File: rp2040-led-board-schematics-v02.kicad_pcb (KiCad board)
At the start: 4 copper layers, 228 x 98 mm, 287 parts, among them J1 ReceiverRS485, J10 Terminal, J11 ReceiverData, J12 ReceiverData, J13 ReceiverData, J14 ReceiverData, J15 ReceiverRS485, J16 ReceiverRS485, J17 ReceiverRS485, J18 ReceiverRS485, J19 Terminal, J2 ReceiverRS485, J20 Terminal, J21 Terminal, J22 Terminal, J23 ReceiverData, J24 ReceiverData, J25 ReceiverData, J26 ReceiverData, J27 MainBoard, J3 ReceiverRS485, J4 ReceiverRS485, J5 PWR_IN, J6 Terminal, J7 Terminal, J8 Terminal, J9 FrontPanel, SW1 PEC16, SW2 Button, U10 MAX485EE, U11 MAX485EE, U12 MAX485EE, U13 MAX485EE, U14 Pico, U15 MAX485EE, U16 MAX485EE, U17 AMS1117-5.0, U21 MAX485EE, U22 MAX485EE, U23 MAX485EE, U24 MAX485EE, U25 MAX485EE, U26 MAX485EE, U27 ENC28J60, U29 AMS1117-5.0, U30 AMS1117-5.0, U31 AMS1117-5.0, U32 AMS1117-5.0, U33 AMS1117-5.0, U34 AMS1117-5.0, U35 AMS1117-5.0, U5 NCP1117LP, U6 MAX485EE, U7 MAX485EE, U8 MAX485EE, U9 MAX485EE

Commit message: should be ready to find parts
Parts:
- removed C16: 220nF, Capacitor_SMD:C_0603_1608Metric
- removed JP5: 12V, Jumper:SolderJumper-2_P1.3mm_Open_Pad1.0x1.5mm
- removed U5: NCP1117LP, Package_TO_SOT_SMD:SOT-223
- added C71: 100nF, Capacitor_SMD:C_0603_1608Metric, F.Cu at (68.0, 80.3)
- added C72: 100nF, Capacitor_SMD:C_0402_1005Metric, F.Cu at (63.0, 77.0)
- added C74: 10uF, Capacitor_SMD:C_1206_3216Metric, F.Cu at (60.0, 73.5)
- added F1: 1A, Fuse:Fuse_1206_3216Metric, F.Cu at (59.8, 64.3)
- added FB2: 600 @ 600Mhz, Inductor_SMD:L_0805_2012Metric, F.Cu at (71.5, 80.6)
- added JPe: 12V, Jumper:SolderJumper-2_P1.3mm_Open_Pad1.0x1.5mm, F.Cu at (56.4, 68.0)
- added L1: 5.6mH 120mOhm, Inductor_SMD:L_Sunlord_MWSA0503S, F.Cu at (69.0, 74.0)
- added Q1: AO3401A, Package_TO_SOT_SMD:SOT-23, F.Cu at (49.9, 69.5)
- added U2: LMR50410Y5FQDBVRQ1, Package_TO_SOT_SMD:SOT-23-6, F.Cu at (63.9, 79.5)
- C11: value 100nF -> 1uF
- moved JP10 22.1 mm to (55.0, 63.0), turned to 180 degrees
- moved C11 11.2 mm to (69.8, 80.3), turned to -90 degrees
- moved H13 8.26 mm to (55.0, 98.0)
- moved J9 4.34 mm to (47.0, 75.3)
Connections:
- C11 pad 1: Net-(JP5-A) -> /Buck in
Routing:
- net Net-(Q1-S): track 0.00 -> 35.5 mm
- net /Buck out: track 0.00 -> 20.1 mm
- net Net-(Q1-D): track 0.00 -> 11.5 mm
- net Net-(J5-Pin_2): track 23.8 -> 14.9 mm
- net Net-(JP5-A): track 6.62 -> 0.00 mm
- net /Receiver 7/12V: track 0.00 -> 6.52 mm
- net /Receiver 5/12V: track 0.00 -> 6.52 mm
- net /Receiver 3/12V: track 0.00 -> 6.52 mm
- net /Receiver 2/12V: track 0.00 -> 6.52 mm
- net /Receiver 1/12V: track 0.00 -> 6.52 mm
- net /Receiver 8/12V: track 0.00 -> 6.52 mm
- net /Receiver 6/12V: track 0.00 -> 6.52 mm
- net /Receiver 4/12V: track 0.00 -> 6.52 mm
- net MBSwitchPush: track 156.6 -> 151.1 mm
- net MBEncoderS: track 104.6 -> 99.5 mm
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- added copper zone on F.Cu, net /Buck in
- added copper zone on F.Cu, net /Buck out
- added copper zone on F.Cu, net /SW
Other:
- board text added: "LED2 STRIP"
- board text added: "LED2-"
- board text added: "LED3 STRIP"
- board text added: "LED3-"
- board text added: "LED4 STRIP"
- board text added: "LED4-"
- board text added: "LED5 STRIP"
- board text added: "LED5-"
- board text added: "LED6 STRIP"
- board text added: "LED6-"
- board text added: "LED7 STRIP"
- board text added: "LED7-"
- board text added: "LED8 STRIP"
- board text added: "LED8-"

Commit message: fix: update .svg & .png files, correct some silkscreen details
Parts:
- moved H34 1.41 mm to (253.5, 70.9)
- moved H35 1.41 mm to (230.5, 70.9)
- moved H36 1.41 mm to (207.5, 70.9)
- moved H37 1.41 mm to (184.5, 71.0)
- moved H38 1.41 mm to (253.5, 114.0)
- moved H39 1.41 mm to (230.5, 114.0)
- moved H40 1.41 mm to (207.5, 114.0)
- moved H41 1.41 mm to (184.5, 114.0)
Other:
- board text added: "LED BOARD [receiver1] v1 - jan 2024"
- board text added: "LED BOARD [receiver2] v1 - jan 2024"
- board text added: "LED BOARD [receiver3] v1 - jan 2024"
- board text added: "LED BOARD [receiver4] v1 - jan 2024"
- board text added: "LED BOARD [receiver5] v1 - jan 2024"
- board text added: "LED BOARD [receiver6] v1 - jan 2024"
- board text added: "LED BOARD [receiver7] v1 - jan 2024"
- board text added: "LED BOARD [receiver8] v1 - jan 2024"
- board text removed: "LED BOARD [receiver] v1 - jan 2024"
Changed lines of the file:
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@@
   )
   (footprint "Frangitron:frangitron_logo_16mm" (layer "B.Cu")
-    (at 185.5 113 90)
+    (at 184.500001 114 90)
     (property "Sheetfile" "Receiver.kicad_sch")
     (property "Sheetname" "Receiver 1")
@@
   )
   (footprint "Frangitron:frangitron_logo_16mm" (layer "B.Cu")
-    (at 185.499999 70 90)
+    (at 184.5 71 90)
     (property "Sheetfile" "Receiver.kicad_sch")
     (property "Sheetname" "Receiver 2")
@@
   )
   (footprint "Frangitron:frangitron_logo_16mm" (layer "B.Cu")
-    (at 254.499999 69.925001 90)
+    (at 253.5 70.925001 90)
     (property "Sheetfile" "Receiver.kicad_sch")
     (property "Sheetname" "Receiver 8")
@@
   )
   (footprint "Frangitron:frangitron_logo_16mm" (layer "B.Cu")
-    (at 231.499999 69.925001 90)
+    (at 230.5 70.925001 90)
     (property "Sheetfile" "Receiver.kicad_sch")
     (property "Sheetname" "Receiver 6")
@@
   )
   (footprint "Frangitron:frangitron_logo_16mm" (layer "B.Cu")
-    (at 231.499999 113 90)
+    (at 230.5 114 90)
     (property "Sheetfile" "Receiver.kicad_sch")
     (property "Sheetname" "Receiver 5")
@@
   )
   (footprint "Frangitron:frangitron_logo_16mm" (layer "B.Cu")
-    (at 208.499999 69.925001 90)
+    (at 207.5 70.925001 90)
     (property "Sheetfile" "Receiver.kicad_sch")
     (property "Sheetname" "Receiver 4")
@@
   )
   (footprint "Frangitron:frangitron_logo_16mm" (layer "B.Cu")
-    (at 208.499999 113 90)
+    (at 207.5 114 90)
     (property "Sheetfile" "Receiver.kicad_sch")
     (property "Sheetname" "Receiver 3")
@@
   )
   (footprint "Frangitron:frangitron_logo_16mm" (layer "B.Cu")
-    (at 254.499999 113 90)
+    (at 253.5 114 90)
     (property "Sheetfile" "Receiver.kicad_sch")
     (property "Sheetname" "Receiver 7")
@@
   (gr_arc locked (start 144.999999 134) (mid 143.24264 138.242641) (end 138.999999 140)
     (stroke (width 0.1) (type default)) (layer "User.2"))
+  (gr_text "LED BOARD [receiver2]\nv1 - jan 2024" (at 180.000001 78.5 270) (layer "B.SilkS")
+    (effects (font (size 0.8 0.8) (thickness 0.15)) (justify left bottom mirror))
+  )
+  (gr_text "LED BOARD [receiver6]\nv1 - jan 2024" (at 226.000001 78.5 270) (layer "B.SilkS")
+    (effects (font (size 0.8 0.8) (thickness 0.15)) (justify left bottom mirror))
+  )
+  (gr_text "LED BOARD [receiver4]\nv1 - jan 2024" (at 203.000001 78.5 270) (layer "B.SilkS")
+    (effects (font (size 0.8 0.8) (thickness 0.15)) (justify left bottom mirror))
+  )
+  (gr_text "LED BOARD [receiver7]\nv1 - jan 2024" (at 249.000001 121.5 270) (layer "B.SilkS")
+    (effects (font (size 0.8 0.8) (thickness 0.15)) (justify left bottom mirror))
+  )
+  (gr_text "LED BOARD [receiver3]\nv1 - jan 2024" (at 203.000001 121.5 270) (layer "B.SilkS")
+    (effects (font (size 0.8 0.8) (thickness 0.15)) (justify left bottom mirror))
+  )
   (gr_text "LED BOARD [front panel]\nv1 - jan 2024" (at 172.999999 113.461592 90) (layer "B.SilkS")
     (effects (font (size 0.8 0.8) (thickness 0.15)) (justify left bottom mirror))
   )
-  (gr_text "LED BOARD [receiver]\nv1 - jan 2024" (at 180.999999 120.499999 -90) (layer "B.SilkS")
+  (gr_text "LED BOARD [receiver8]\nv1 - jan 2024" (at 249.000001 78.5 270) (layer "B.SilkS")
+    (effects (font (size 0.8 0.8) (thickness 0.15)) (justify left bottom mirror))
+  )
+  (gr_text "LED BOARD [receiver5]\nv1 - jan 2024" (at 226.000001 121.5 270) (layer "B.SilkS")
+    (effects (font (size 0.8 0.8) (thickness 0.15)) (justify left bottom mirror))
+  )
+  (gr_text "LED BOARD [receiver1]\nv1 - jan 2024" (at 180 121.499999 270) (layer "B.SilkS")
     (effects (font (size 0.8 0.8) (thickness 0.15)) (justify left bottom mirror))
   )

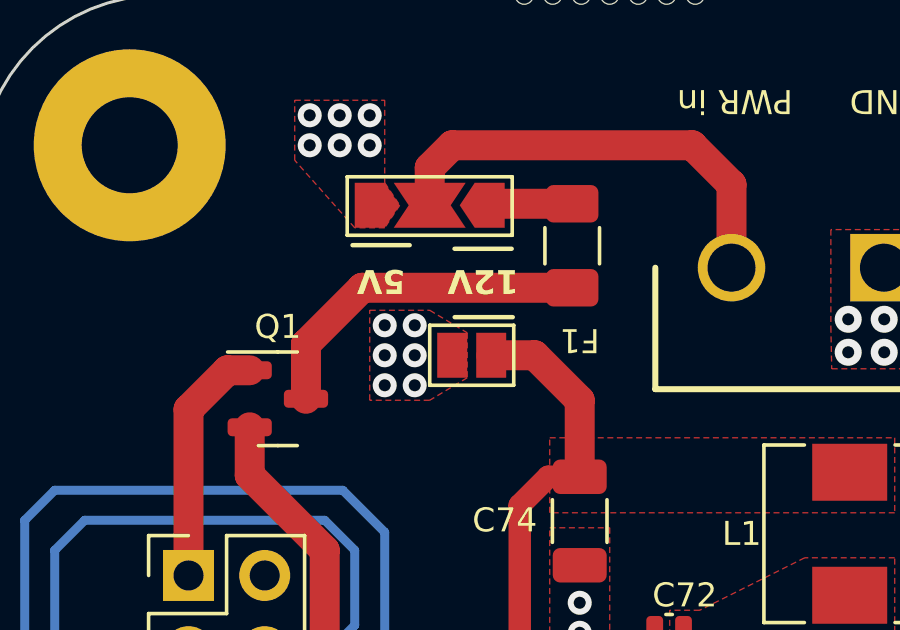
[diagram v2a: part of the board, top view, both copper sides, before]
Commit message: fix: DRC & ERC revealed designators were out of sync between schem and pcb
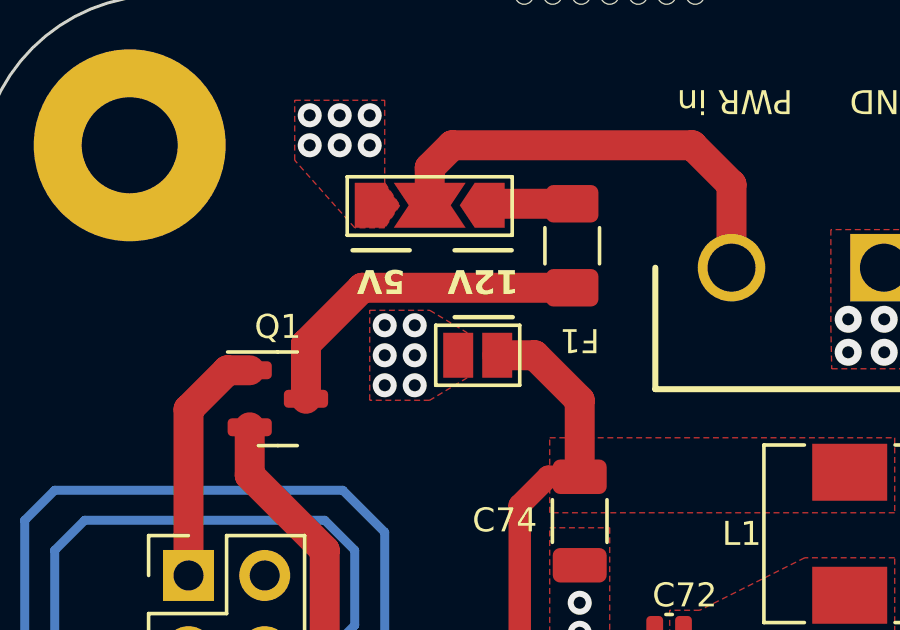
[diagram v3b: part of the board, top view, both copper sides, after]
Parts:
- removed JPe: 12V, Jumper:SolderJumper-2_P1.3mm_Open_Pad1.0x1.5mm
- added JP5: 12V, Jumper:SolderJumper-2_P1.3mm_Open_Pad1.0x1.5mm, F.Cu at (56.6, 68.0)
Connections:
- net Net-(U2-CB) renamed /CB
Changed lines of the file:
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@@
   (net 156 "/Receiver 7/LDO OUT")
   (net 157 "/Buck in")
-  (net 158 "Net-(U2-CB)")
+  (net 158 "/CB")
   (net 159 "/Buck out")
   (net 160 "Net-(Q1-S)")
@@
       (net 162 "/SW") (pintype "passive"))
     (pad "2" smd roundrect (at 0.48 0 180) (size 0.56 0.62) (layers "F.Cu" "F.Paste" "F.Mask") (roundrect_rratio 0.25)
-      (net 158 "Net-(U2-CB)") (pintype "passive"))
+      (net 158 "/CB") (pintype "passive"))
     (model "${KICAD6_3DMODEL_DIR}/Capacitor_SMD.3dshapes/C_0402_1005Metric.wrl"
       (offset (xyz 0 0 0))
@@
       (net 11 "/FP GND") (pinfunction "1") (pintype "input"))
   )
-  (footprint "Jumper:SolderJumper-2_P1.3mm_Open_Pad1.0x1.5mm" (layer "F.Cu")
-    (at 56.4 68 180)
-    (descr "SMD Solder Jumper, 1x1.5mm Pads, 0.3mm gap, open")
-    (tags "solder jumper open")
-    (property "Sheetfile" "rp2040-led-board-schematics-v02.kicad_sch")
-    (property "Sheetname" "")
-    (property "URL" "")
-    (property "ki_description" "Solder Jumper, 2-pole, open")
-    (property "ki_keywords" "solder jumper SPST")
-    (attr exclude_from_pos_files)
-    (fp_text reference "JPe" (at 0 -1.8) (layer "F.SilkS") hide
-        (effects (font (size 0.8 0.8) (thickness 0.15)))
-    )
-    (fp_text value "12V" (at 0 1.9) (layer "F.Fab")
-        (effects (font (size 0.8 0.8) (thickness 0.15)))
-    )
-    (fp_line (start -1.4 -1) (end 1.4 -1)
-      (stroke (width 0.12) (type solid)) (layer "F.SilkS"))
-    (fp_line (start -1.4 1) (end -1.4 -1)
-      (stroke (width 0.12) (type solid)) (layer "F.SilkS"))
-    (fp_line (start 1.4 -1) (end 1.4 1)
-      (stroke (width 0.12) (type solid)) (layer "F.SilkS"))
-    (fp_line (start 1.4 1) (end -1.4 1)
-      (stroke (width 0.12) (type solid)) (layer "F.SilkS"))
-    (fp_line (start -1.65 -1.25) (end -1.65 1.25)
-      (stroke (width 0.05) (type solid)) (layer "F.CrtYd"))
-    (fp_line (start -1.65 -1.25) (end 1.65 -1.25)
-      (stroke (width 0.05) (type solid)) (layer "F.CrtYd"))
-    (fp_line (start 1.65 1.25) (end -1.65 1.25)
-      (stroke (width 0.05) (type solid)) (layer "F.CrtYd"))
-    (fp_line (start 1.65 1.25) (end 1.65 -1.25)
-      (stroke (width 0.05) (type solid)) (layer "F.CrtYd"))
-    (pad "1" smd rect (at -0.65 0 180) (size 1 1.5) (layers "F.Cu" "F.Mask")
-      (net 159 "/Buck out") (pinfunction "A") (pintype "passive"))
-    (pad "2" smd rect (at 0.65 0 180) (size 1 1.5) (layers "F.Cu" "F.Mask")
-      (net 41 "+5V") (pinfunction "B") (pintype "passive"))
-  )
   (footprint "Resistor_SMD:R_0402_1005Metric" (layer "F.Cu")
     (at 130.715999 106.753 90)
@@
       (stroke (width 0.1) (type solid)) (layer "F.Fab"))
     (pad "1" smd roundrect (at -1.1375 -0.95) (size 1.325 0.6) (layers "F.Cu" "F.Paste" "F.Mask") (roundrect_rratio 0.25)
-      (net 158 "Net-(U2-CB)") (pinfunction "CB") (pintype "power_in"))
+      (net 158 "/CB") (pinfunction "CB") (pintype "power_in"))
     (pad "2" smd roundrect (at -1.1375 0) (size 1.325 0.6) (layers "F.Cu" "F.Paste" "F.Mask") (roundrect_rratio 0.25)
       (net 2 "GND") (pinfunction "GND") (pintype "power_in"))
@@
     )
   )
+  (footprint "Jumper:SolderJumper-2_P1.3mm_Open_Pad1.0x1.5mm" (layer "F.Cu")
+    (at 56.6 68 180)
+    (descr "SMD Solder Jumper, 1x1.5mm Pads, 0.3mm gap, open")
+    (tags "solder jumper open")
+    (property "Sheetfile" "rp2040-led-board-schematics-v02.kicad_sch")
+    (property "Sheetname" "")
+    (property "URL" "")
+    (property "ki_description" "Solder Jumper, 2-pole, open")
+    (property "ki_keywords" "solder jumper SPST")
+    (attr exclude_from_pos_files)
+    (fp_text reference "JP5" (at 0 -1.8) (layer "F.SilkS") hide
+        (effects (font (size 1 1) (thickness 0.15)))
+    )
+    (fp_text value "12V" (at 0 1.9) (layer "F.Fab")
+        (effects (font (size 1 1) (thickness 0.15)))
+    )
+    (fp_line (start -1.4 -1) (end 1.4 -1)
+      (stroke (width 0.12) (type solid)) (layer "F.SilkS"))
+    (fp_line (start -1.4 1) (end -1.4 -1)
+      (stroke (width 0.12) (type solid)) (layer "F.SilkS"))
+    (fp_line (start 1.4 -1) (end 1.4 1)
+      (stroke (width 0.12) (type solid)) (layer "F.SilkS"))
+    (fp_line (start 1.4 1) (end -1.4 1)
+      (stroke (width 0.12) (type solid)) (layer "F.SilkS"))
+    (fp_line (start -1.65 -1.25) (end -1.65 1.25)
+      (stroke (width 0.05) (type solid)) (layer "F.CrtYd"))
+    (fp_line (start -1.65 -1.25) (end 1.65 -1.25)
+      (stroke (width 0.05) (type solid)) (layer "F.CrtYd"))
+    (fp_line (start 1.65 1.25) (end -1.65 1.25)
+      (stroke (width 0.05) (type solid)) (layer "F.CrtYd"))
+    (fp_line (start 1.65 1.25) (end 1.65 -1.25)
+      (stroke (width 0.05) (type solid)) (layer "F.CrtYd"))
+    (pad "1" smd rect (at -0.65 0 180) (size 1 1.5) (layers "F.Cu" "F.Mask")
+      (net 159 "/Buck out") (pinfunction "A") (pintype "passive"))
+    (pad "2" smd rect (at 0.65 0 180) (size 1 1.5) (layers "F.Cu" "F.Mask")
+      (net 41 "+5V") (pinfunction "B") (pintype "passive"))
+  )
   (footprint "Resistor_SMD:R_0402_1005Metric" (layer "F.Cu")
     (at 88.238999 120.33 -90)
@@
   (gr_line (start 259.804999 108) (end 257.594999 108)
     (stroke (width 0.15) (type default)) (layer "F.SilkS"))
-  (gr_line (start 55.8275 64.45) (end 57.7325 64.45)
+  (gr_line (start 55.8275 64.5) (end 57.7325 64.5)
     (stroke (width 0.15) (type default)) (layer "F.SilkS"))
   (gr_line (start 183.499999 65.63) (end 183.499999 68.17)
@@
   (gr_line (start 229.499999 108.63) (end 229.499999 111.17)
     (stroke (width 0.15) (type default)) (layer "F.SilkS"))
-  (gr_line (start 52.4275 64.33) (end 54.3325 64.33)
+  (gr_line (start 52.4275 64.5) (end 54.3325 64.5)
     (stroke (width 0.15) (type default)) (layer "F.SilkS"))
   (gr_line (start 229.499999 65.555001) (end 229.499999 68.095001)
@@
   (segment (start 62.5 78.325) (end 62.725 78.55) (width 0.5) (layer "F.Cu") (net 158))
   (segment (start 62.5 77) (end 62.5 78.325) (width 0.5) (layer "F.Cu") (net 158))
-  (segment (start 57.05 68) (end 58.5 68) (width 1) (layer "F.Cu") (net 159))
   (segment (start 58 73) (end 58.95 72.05) (width 0.75) (layer "F.Cu") (net 159))
+  (segment (start 58.5 68) (end 57.25 68) (width 1) (layer "F.Cu") (net 159))
+  (segment (start 60 69.5) (end 60 72.05) (width 1) (layer "F.Cu") (net 159))
   (segment (start 62.725 80.45) (end 58.95 80.45) (width 0.75) (layer "F.Cu") (net 159))
+  (segment (start 58.5 68) (end 60 69.5) (width 1) (layer "F.Cu") (net 159))
   (segment (start 58 79.5) (end 58 73) (width 0.75) (layer "F.Cu") (net 159))
   (segment (start 58.95 80.45) (end 58 79.5) (width 0.75) (layer "F.Cu") (net 159))
-  (segment (start 60 69.5) (end 60 72.05) (width 1) (layer "F.Cu") (net 159))
   (segment (start 58.95 72.05) (end 60 72.05) (width 0.75) (layer "F.Cu") (net 159))
-  (segment (start 58.5 68) (end 60 69.5) (width 1) (layer "F.Cu") (net 159))
   (segment (start 51.5 83) (end 51.5 74.5) (width 1) (layer "F.Cu") (net 160))
   (segment (start 51.5 74.5) (end 49 72) (width 1) (layer "F.Cu") (net 160))
@@
         (xy 194.249999 75.500001)
         (xy 194.249998 75.500001)
-        (xy 194.249998 75.500001)
-        (xy 194.249998 75.500001)
         (xy 194.249998 66.750001)
         (xy 181.499998 66.750001)
@@
         (xy 194.25 118.500001)
         (xy 194.249999 118.500001)
-        (xy 194.249999 118.500001)
-        (xy 194.249999 118.500001)
         (xy 194.249999 109.750001)
         (xy 181.499999 109.750001)
@@
         (xy 217.249999 118.500001)
         (xy 217.249998 118.500001)
-        (xy 217.249998 118.500001)
-        (xy 217.249998 118.500001)
         (xy 217.249998 109.750001)
         (xy 204.499998 109.750001)
@@
         (xy 240.249999 75.425002)
         (xy 240.249998 75.425002)
-        (xy 240.249998 75.425002)
-        (xy 240.249998 75.425002)
         (xy 240.249998 66.675002)
         (xy 227.499998 66.675002)
@@
         (xy 263.249999 118.500001)
         (xy 263.249998 118.500001)
-        (xy 263.249998 118.500001)
-        (xy 263.249998 118.500001)
         (xy 263.249998 109.750001)
         (xy 250.499998 109.750001)
@@
         (xy 240.249999 118.500001)
         (xy 240.249998 118.500001)
-        (xy 240.249998 118.500001)
-        (xy 240.249998 118.500001)
         (xy 240.249998 109.750001)
         (xy 227.499998 109.750001)
@@
         (xy 263.249999 75.425002)
         (xy 263.249998 75.425002)
-        (xy 263.249998 75.425002)
-        (xy 263.249998 75.425002)
         (xy 263.249998 66.675002)
         (xy 250.499998 66.675002)
@@
         (xy 217.249999 75.425002)
         (xy 217.249998 75.425002)
-        (xy 217.249998 75.425002)
-        (xy 217.249998 75.425002)
         (xy 217.249998 66.675002)
